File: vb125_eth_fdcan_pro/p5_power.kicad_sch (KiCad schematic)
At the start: 0 parts

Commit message: AOZ schematic. 3V3 DC-DC. Partly bus power.
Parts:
- added C1 (x2): 10uF, symbol Device:C
- added C1: 100nF, symbol Device:C
- added C1: 3.3nF, symbol Device:C
- added C1 (x2): DNP, symbol Device:C
- added C1: >10uF, symbol Device:C
- added L2: DFE252010F-1R0M=P2, Inductor_SMD:L_1008_2520Metric, symbol Device:L_Iron
- added R19: 0, Resistor_SMD:R_0402_1005Metric, symbol Device:R
- added R19: 45k, Resistor_SMD:R_0402_1005Metric, symbol Device:R
- added R19: 10k, Resistor_SMD:R_0402_1005Metric, symbol Device:R
- added R19 (x2): 100K, Resistor_SMD:R_0402_1005Metric, symbol Device:R
- added R19: 301K, Resistor_SMD:R_0402_1005Metric, symbol Device:R
- added U4: AOZ1282CI, Package_TO_SOT_SMD:SOT-23-6, symbol Regulator_Switching:AOZ1282CI
- added U5: AOZ1376DI-02, symbol vhrd_pmic_switch:AOZ1376DI
- added U6: RT5760A/B, Package_TO_SOT_SMD:SOT-563, symbol vhrd_pmic_regulator:RT5760
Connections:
- new net +3V3_DCDC: C1.1, C1.1, L2.2, R19.2, R19.2
- new net +5V0_SYS: C1.1, C1.1, C1.1, R19.2, U5.1 (VOUT), U5.2 (VOUT), U6.3 (VIN), U6.5 (EN)
- new net +VIN_USB: C1.1, U5.11 (VIN), U5.12 (VIN)
- new net 3V3_FB: C1.2, R19.1, R19.2, U6.1 (FB)
- new net 3V3_PG: R19.1, U6.6 (PG)
- new net 3V3_SW: L2.1, U6.4 (SW)
- new net AOZ_ENB: R19.1, U5.5 (ENB)
- new net AOZ_POVP: R19.1, U5.3 (POVP)
- new net AOZ_SS: C1.1, U5.7 (SS)
- new net GND: C1.2, C1.2, C1.2, C1.2, C1.2, C1.2, R19.1, R19.2, R19.2, U5.13 (EP_GND), U5.6 (GND), U6.2 (GND)
- new net VUSB_FLTB: R19.1, U5.4 (FLTB)
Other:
- note added: "+3V3 DC-DC"
- note added: "USB OVP/RB/UVP/SC"

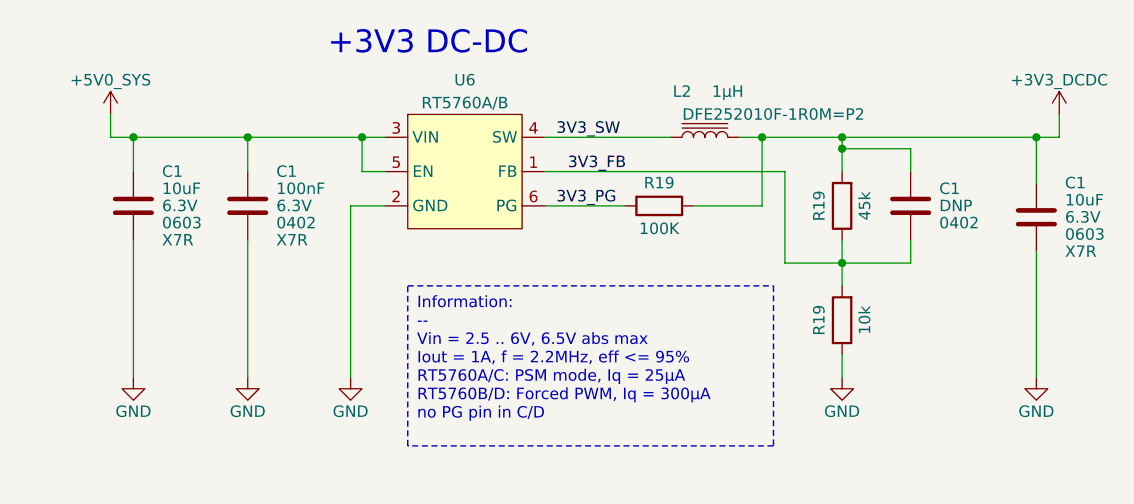
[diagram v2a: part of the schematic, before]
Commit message: CAN schematics. Assign IO on H7.
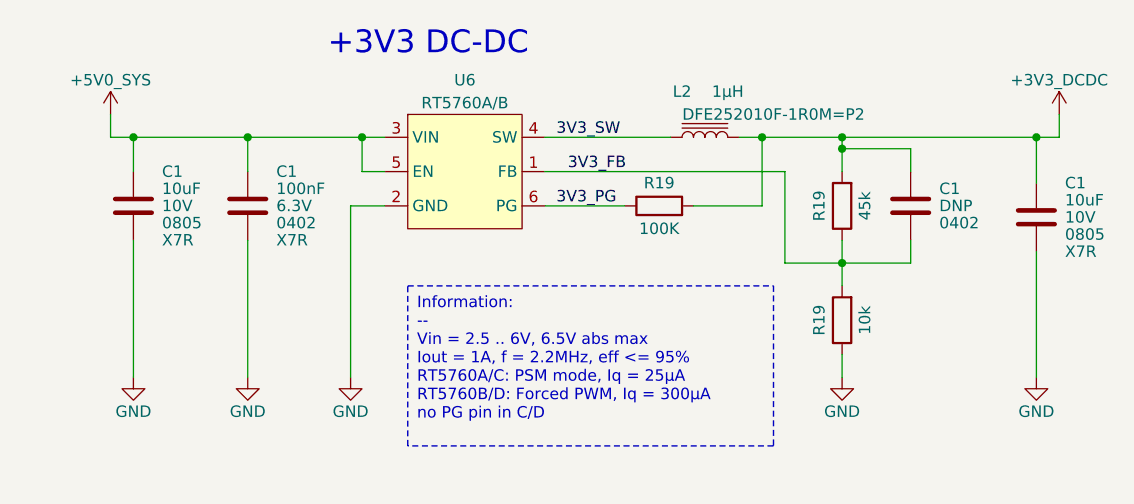
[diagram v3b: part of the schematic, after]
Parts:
- removed C1 (x2): 10uF, symbol Device:C
- added C1 (x2): 10uF, Capacitor_SMD:C_0805_2012Metric, symbol Device:C
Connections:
- net +3V3_DCDC: now also C1.1
- net +5V0_SYS: now also C1.1
- net GND: now also C1.2, C1.2

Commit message: Finish schematics.
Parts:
- removed U4: AOZ1282CI, Package_TO_SOT_SMD:SOT-23-6, symbol Regulator_Switching:AOZ1282CI
- added NT1: NetTie_2, symbol Device:NetTie_2
- C1: footprint (none) -> Capacitor_SMD:C_0402_1005Metric
- C1: footprint (none) -> Capacitor_SMD:C_0603_1608Metric
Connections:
- net GND: now also NT1.2
- new net CHASSIS: NT1.1
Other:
- note added: "Chassis to GND"
- moved on the sheet: C1, L2, R19, U5, U6

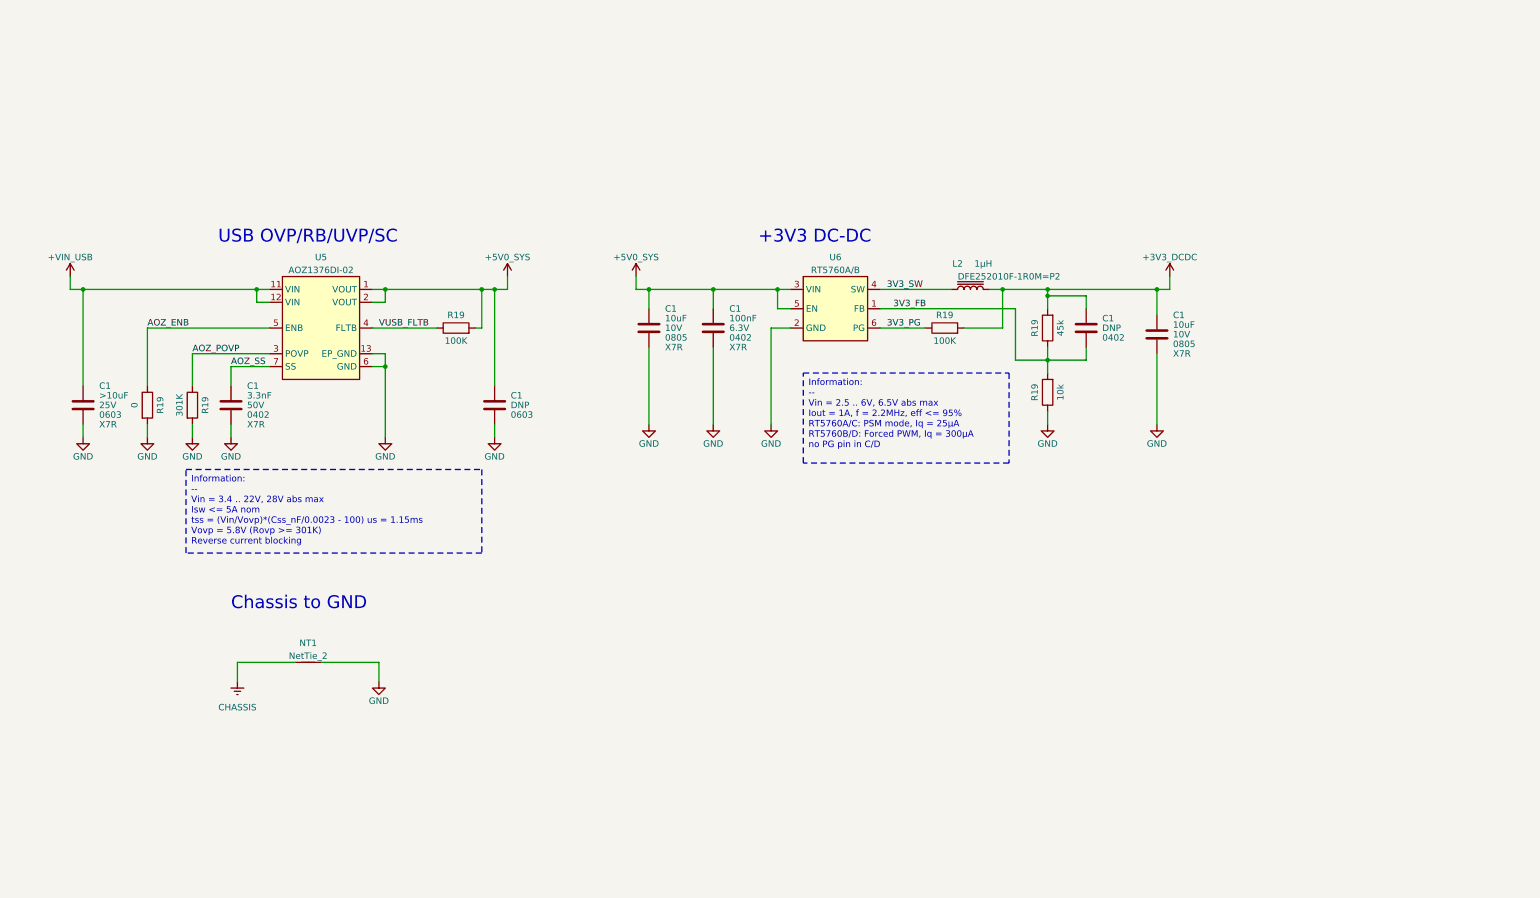
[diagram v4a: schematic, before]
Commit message: Add testpoints and set page templates.
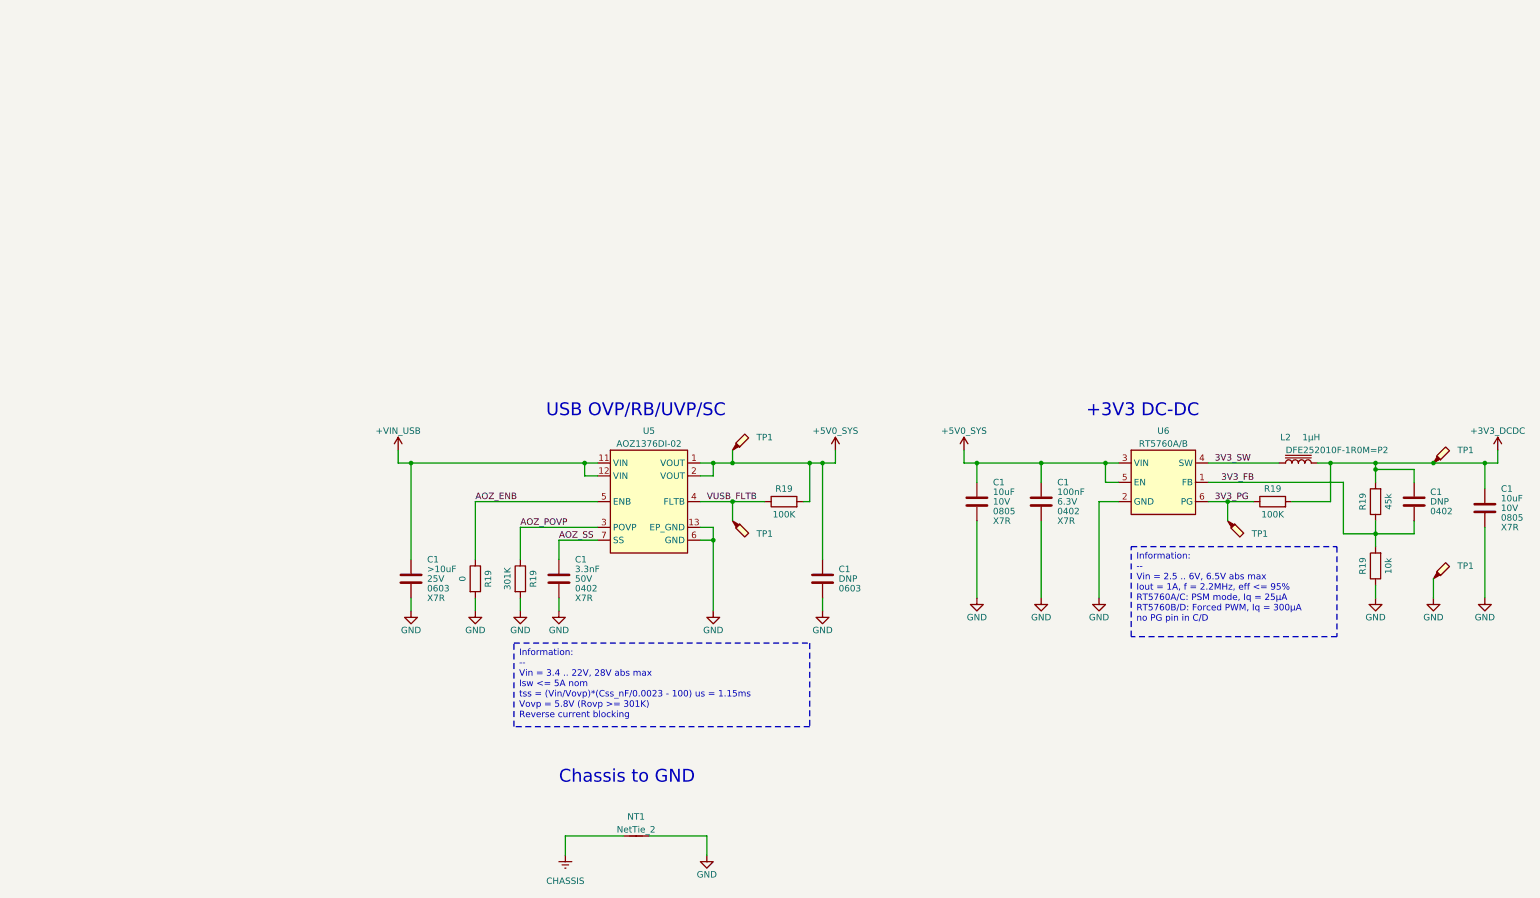
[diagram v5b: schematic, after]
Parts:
- added TP1 (x5): TestPoint_Probe, TestPoint:TestPoint_Pad_D1.5mm, symbol Connector:TestPoint_Probe
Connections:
- net +3V3_DCDC: now also TP1.1
- net +5V0_SYS: now also TP1.1
- net 3V3_PG: now also TP1.1
- net GND: now also TP1.1
- net VUSB_FLTB: now also TP1.1
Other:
- company: (none) -> vhrd.tech AS
- title: (none) -> rt_bridge_pro
- moved on the sheet: C1, L2, NT1, R19, U5, U6

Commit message: Add sourcing information for resistors
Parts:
- R19: Mpn1 (none) -> RMCF0402FT10K0; Mpn2 (none) -> CR0402-FX-1002GLF
- R19: Mpn1 (none) -> RMCF0402FT100K; Mpn2 (none) -> CR0402-FX-1003GLF
- R19: Mpn1 (none) -> RMCF0402FT301K; Mpn2 (none) -> RC0402FR-07301KL
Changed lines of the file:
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@@
+      (effects (font (size 1.27 1.27)) hide)
+    )
+    (property "Mpn1" "RMCF0402FT10K0" (at 293.37 132.08 0)
+      (effects (font (size 1.27 1.27)) hide)
+    )
+    (property "Mpn2" "CR0402-FX-1002GLF" (at 293.37 132.08 0)
       (effects (font (size 1.27 1.27)) hide)
     )
@@
     )
     (property "Datasheet" "~" (at 273.05 119.38 0)
+      (effects (font (size 1.27 1.27)) hide)
+    )
+    (property "Mpn1" "RMCF0402FT100K" (at 273.05 119.38 0)
+      (effects (font (size 1.27 1.27)) hide)
+    )
+    (property "Mpn2" "CR0402-FX-1003GLF" (at 273.05 119.38 0)
       (effects (font (size 1.27 1.27)) hide)
     )
@@
     )
     (property "Datasheet" "~" (at 176.53 119.38 0)
+      (effects (font (size 1.27 1.27)) hide)
+    )
+    (property "Mpn1" "RMCF0402FT100K" (at 176.53 119.38 0)
+      (effects (font (size 1.27 1.27)) hide)
+    )
+    (property "Mpn2" "CR0402-FX-1003GLF" (at 176.53 119.38 0)
       (effects (font (size 1.27 1.27)) hide)
     )
@@
       (effects (font (size 1.27 1.27)) hide)
     )
+    (property "Mpn1" "RMCF0402FT301K" (at 124.46 134.62 0)
+      (effects (font (size 1.27 1.27)) hide)
+    )
+    (property "Mpn2" "RC0402FR-07301KL" (at 124.46 134.62 0)
+      (effects (font (size 1.27 1.27)) hide)
+    )

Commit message: Selection of capacitors for VB125
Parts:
- C1: Mpn1 (none) -> Samsung:CL05B104KQ5NNNC; Mpn2 (none) -> YAGEO:CC0402KRX7R5BB104
- C1: Mpn1 (none) -> CL05B332KB5NNNC; Mpn2 (none) -> CC0402KRX7R9BB332
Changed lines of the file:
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@@
+      (effects (font (size 1.27 1.27)) hide)
+    )
+    (property "Mpn1" "Samsung:CL05B104KQ5NNNC  " (at 227.33 119.38 0)
+      (effects (font (size 1.27 1.27)) hide)
+    )
+    (property "Mpn2" "YAGEO:CC0402KRX7R5BB104" (at 227.33 119.38 0)
       (effects (font (size 1.27 1.27)) hide)
     )
@@
       (effects (font (size 1.27 1.27)) hide)
     )
+    (property "Mpn1" "CL05B332KB5NNNC" (at 132.08 134.62 0)
+      (effects (font (size 1.27 1.27)) hide)
+    )
+    (property "Mpn2" "CC0402KRX7R9BB332" (at 132.08 134.62 0)
+      (effects (font (size 1.27 1.27)) hide)
+    )

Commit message: Add missing footprints, ready to layout.
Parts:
- NT1: footprint (none) -> NetTie:NetTie-2_SMD_Pad2.0mm
- U5: footprint (none) -> vhrd_generic:DFN-12-AOZ
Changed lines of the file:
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@@
       (effects (font (size 1.27 1.27)))
     )
-    (property "Footprint" "" (at 147.32 185.42 0)
+    (property "Footprint" "NetTie:NetTie-2_SMD_Pad2.0mm" (at 147.32 185.42 0)
       (effects (font (size 1.27 1.27)) hide)
     )
@@
       (effects (font (size 1.27 1.27)))
     )
-    (property "Footprint" "" (at 142.24 109.22 0)
+    (property "Footprint" "vhrd_generic:DFN-12-AOZ" (at 142.24 109.22 0)
       (effects (font (size 1.27 1.27)) hide)
     )
@@
     (pin "6")
     (pin "7")
+    (pin "10")
+    (pin "8")
+    (pin "9")
     (instances
       (project "vb125_eth_fdcan_pro"
